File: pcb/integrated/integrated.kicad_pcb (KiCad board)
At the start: 4 copper layers, 200 x 100 mm, 264 parts, among them J10001 Conn_01x01_Female, J10002 Conn_01x01_Female, J1001 mounting-hole-grounded, J1002 mounting-hole-grounded, J1003 mounting-hole-grounded, J1004 mounting-hole-grounded, J1005 mounting-hole-grounded, J1006 mounting-hole-grounded, J3001 Conn_01x04_Male, J3002 Conn_01x06_Male, J5001 Conn_Coaxial, J8001 Conn_01x03_Female, Q10001 F423MR12W1M1B11BOMA1, Q8001 Q_NMOS_GDS, Q8002 2N7002, Q8003 Q_NMOS_GDS, U11001 UCC5350SB, U11002 R15P21503D, U12001 UCC5350SB, U12002 R15P21503D, U13001 UCC5350SB, U13002 R15P21503D, U14001 UCC5350SB, U14002 R15P21503D, U3001 XC7S25-L1FTGB196, U3002 S25FL127SABN, U3003 74AVC4TD245BQ, U5001 74LVC1G3157GW, U5002 TLV3501AIDBVR, U5003 74LVC1G3157GW, U5004 MCP6561-OT, U6001 SG3225, U6002 AD9609, U7001 AFBR-1624Z, U7002 AFBR-2624Z, U8001 VOM1271, U8002 UCC5350SB, U8003 ACS730, U9001 EC6AW, U9002 RAC10, U9003 TPS82140, U9004 TPS82140, U9005 TPS735, U9006 TPS735

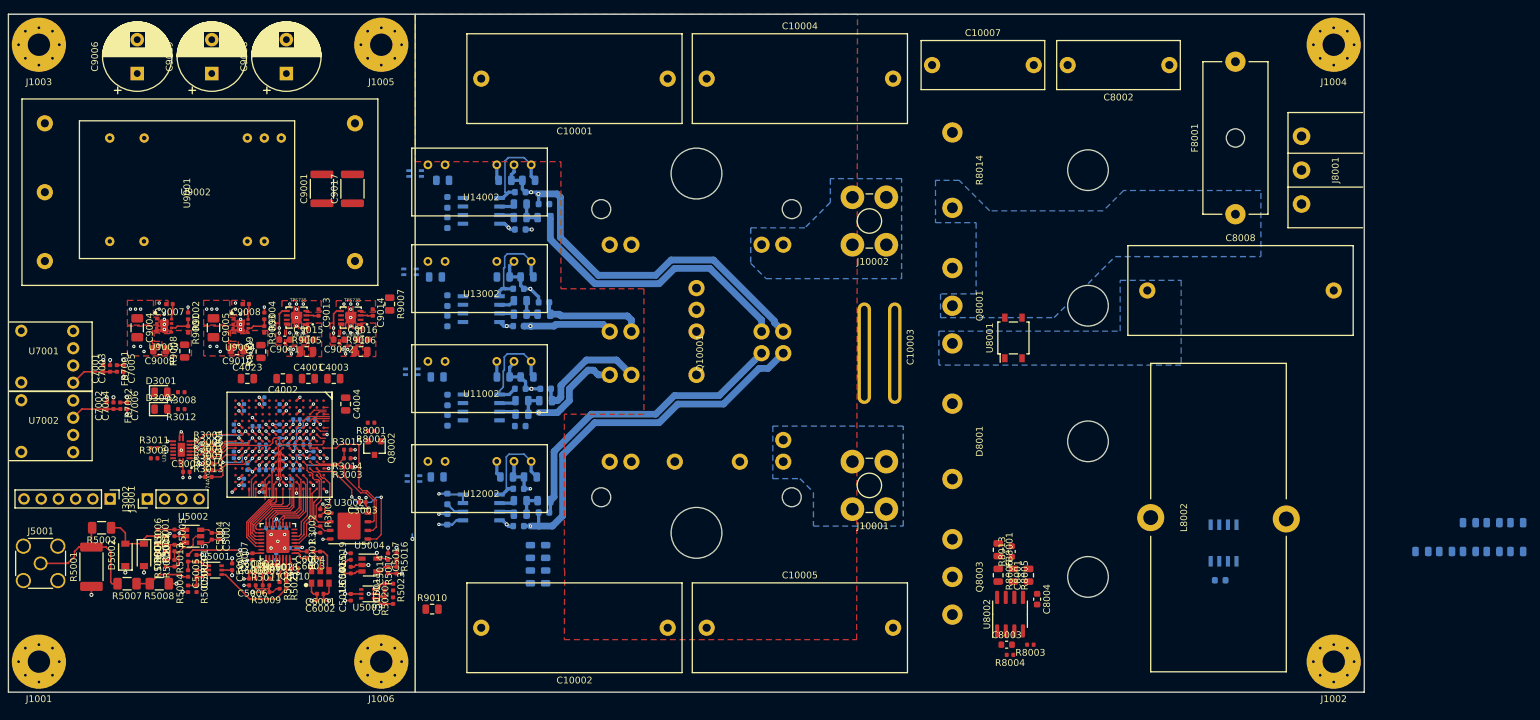
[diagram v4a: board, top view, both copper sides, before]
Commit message: redid power planes
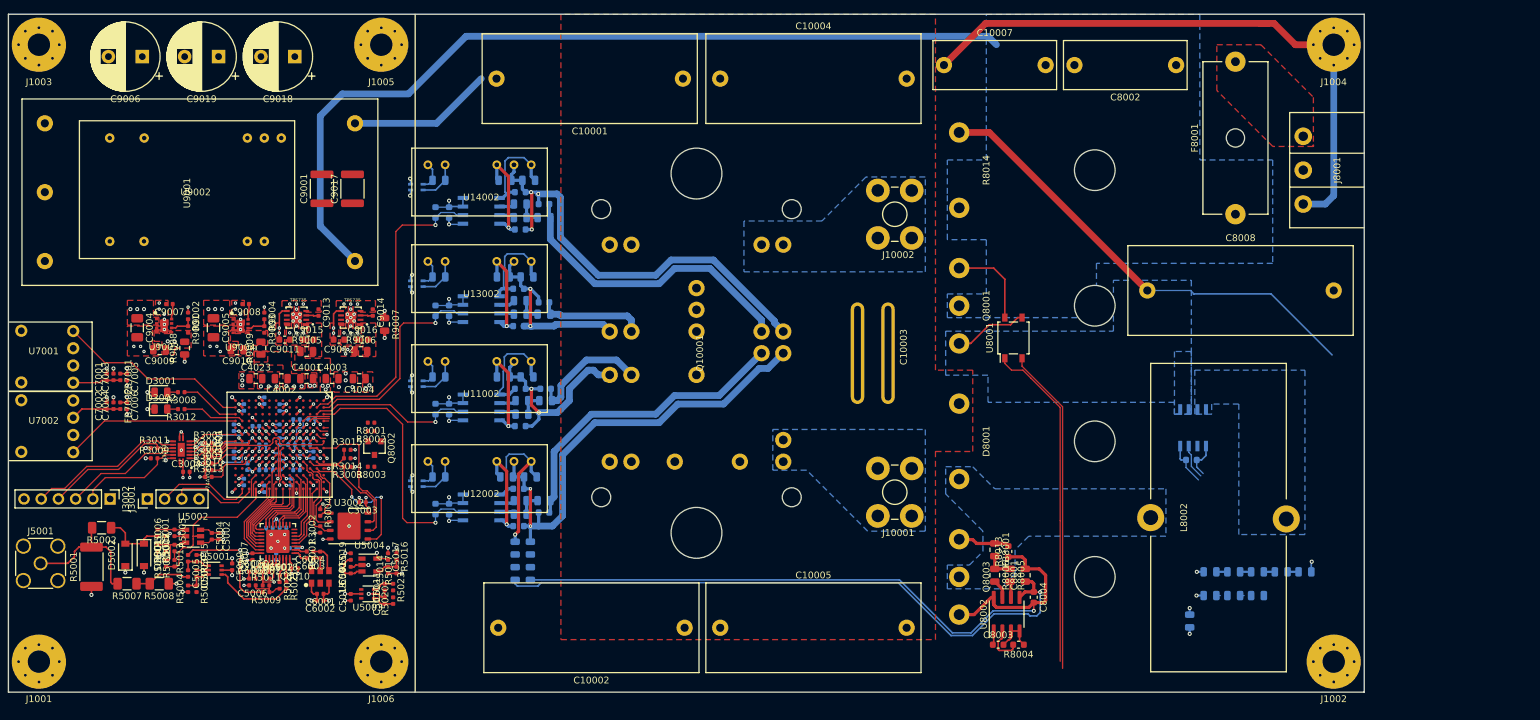
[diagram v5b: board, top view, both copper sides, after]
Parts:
- R8004: footprint Resistor_SMD:R_0402_1005Metric -> Resistor_SMD:R_0603_1608Metric
- R9010: moved to B.Cu
- moved R9010 111.8 mm to (224.2, 139.5), turned to 90 degrees
- moved R8003 100.7 mm to (103.5, 116.8)
- moved R8011 46.5 mm to (227.2, 135.8), turned to 180 degrees
- moved R10007 45.3 mm to (227.2, 132.2), turned to 180 degrees
- moved R8010 39.7 mm to (230.8, 135.8), turned to 180 degrees
- moved R10004 38.4 mm to (230.8, 132.2), turned to 180 degrees
- moved R8007 33.0 mm to (234.2, 135.8), turned to 180 degrees
- moved R10003 31.4 mm to (234.2, 132.2), turned to 180 degrees
- moved R10002 24.4 mm to (237.8, 132.2), turned to 180 degrees
- moved C8005 18.3 mm to (224.5, 115.8)
- moved U8003 17.6 mm to (224.8, 111.0)
- moved R10001 17.5 mm to (241.2, 132.2), turned to 180 degrees
- moved FB12002 4.53 mm to (124.8, 128.8)
- moved R12005 4.53 mm to (124.8, 132.5), turned to 90 degrees
- moved C4004 4.25 mm to (101.8, 103.8), turned to 180 degrees
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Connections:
- C8002 pad 1: VIN -> VLINK
- C8008 pad 1: /Power Input/S1 -> VIN
- C9001 pad 1: VIN -> VLINK
- C9017 pad 1: VIN -> VLINK
- F8001 pad 1: VIN -> VLINK
- Q8001 pad 2: VIN -> VLINK
- Q8001 pad 3: /Power Input/S1 -> VIN
- R11001 pad 2: /Inverter/Gate Drive 1/In -> GATE1
- R12001 pad 2: /Inverter/Gate Drive 2/In -> GATE2
- R13001 pad 2: /Inverter/Gate Drive 3/In -> GATE3
- R14001 pad 2: /Inverter/Gate Drive 4/In -> GATE4
- R8014 pad 1: /Power Input/S1 -> VIN
- R8014 pad 2: VIN -> VLINK
- U11001 pad 2: /Inverter/Gate Drive 1/In -> GATE1
- U12001 pad 2: /Inverter/Gate Drive 2/In -> GATE2
- U13001 pad 2: /Inverter/Gate Drive 3/In -> GATE3
- U14001 pad 2: /Inverter/Gate Drive 4/In -> GATE4
- U3001 pad A2: Net-(U3001-PadA2) -> GATE3
- U3001 pad A3: Net-(U3001-PadA3) -> GATE2
- U3001 pad B2: Net-(U3001-PadB2) -> GATE4
- U3001 pad B3: Net-(U3001-PadB3) -> GATE1
- U3001 pad L14: Net-(U3001-PadL14) -> ZCS_DETECT
- U3001 pad M14: Net-(U3001-PadM14) -> /Control/FPGA/DEBUG_RX
- U3001 pad N14: Net-(U3001-PadN14) -> /Control/FPGA/DEBUG_TX
- U3001 pad N4: Net-(U3001-PadN4) -> /Control/FPGA/LED2
- U3001 pad P2: Net-(U3001-PadP2) -> FIBER_TX
- U3001 pad P3: Net-(U3001-PadP3) -> /Control/FPGA/LED1
- U3001 pad P4: Net-(U3001-PadP4) -> FIBER_RX
- U8001 pad 3: /Power Input/S1 -> VIN
- U8003 pad 1: /Power Input/S1 -> VIN
- U8003 pad 2: /Power Input/S1 -> VIN
- U9001 pad 22: VIN -> VLINK
- U9001 pad 23: VIN -> VLINK
- U9002 pad 1: VIN -> VLINK
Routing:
- net PWRGND: track 0.00 -> 130.7 mm, vias 0 -> 4
- net VLINK: track 0.00 -> 128.7 mm
- net DRIVE_AUX+: track 0.00 -> 92.3 mm, vias 0 -> 1
- net Earth: track 0.00 -> 90.0 mm
- net VIN: track 0.00 -> 80.6 mm
- net Net-(R8003-Pad1): track 0.00 -> 49.1 mm
- net Net-(Q8002-Pad3): track 0.00 -> 48.2 mm
- net GATE4: track 0.00 -> 46.8 mm, vias 0 -> 1
- net GND: track 114.4 -> 161.2 mm, vias 130 -> 159
- net GATE2: track 0.00 -> 37.7 mm, vias 0 -> 1
- net GATE3: track 0.00 -> 31.7 mm, vias 0 -> 1
- net FIBER_TX: track 0.00 -> 28.6 mm
- net FIBER_RX: track 0.00 -> 25.8 mm
- net GATE1: track 0.00 -> 24.8 mm, vias 0 -> 1
- net Net-(J3002-Pad5): track 0.00 -> 23.2 mm
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- added copper zone on In2.Cu, net +12V
- added copper zone on In2.Cu, net +3V3
- added copper zone on In2.Cu, net /Power Rails/12_INT
- added copper zone on F.Cu, net /Power Rails/1_INT
- added copper zone on In2.Cu, net /Power Rails/5_INT
- added copper zone on B.Cu, net Net-(D8001-Pad2)
- added copper zone on F.Cu, net Net-(F8001-Pad2)
- added copper zone on B.Cu, net Net-(L8002-Pad1)
- added copper zone on In1.Cu, net PWRGND
- added copper zone on In2.Cu, net VBUS
- added copper zone on B.Cu, net VLINK
- removed copper zone on F.Cu, net +5V
- removed copper zone on B.Cu, net /Power Input/S1
- removed copper zone on In1.Cu, net GNDPWR

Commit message: PCB routing finihsed, ready for design review
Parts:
- added R5024: 33, Resistor_SMD:R_0402_1005Metric, F.Cu at (110.0, 134.5)
- added R5025: 33, Resistor_SMD:R_0402_1005Metric, F.Cu at (108.8, 134.5)
- added R5026: 33, Resistor_SMD:R_0402_1005Metric, F.Cu at (99.2, 134.0)
- added R5027: 33, Resistor_SMD:R_0402_1005Metric, F.Cu at (100.5, 134.0)
- C9001, C9017: moved to B.Cu
- R8005, R8006: value 1 -> 4.7
- moved C9001 4.47 mm to (100.2, 77.8), turned to 0 degrees
- moved R10001 3.75 mm to (241.2, 136.0)
- moved R10002 3.75 mm to (237.8, 136.0)
- moved R10003 3.75 mm to (234.2, 136.0)
- moved R10004 3.75 mm to (230.8, 136.0)
- moved R10007 3.75 mm to (227.2, 136.0)
- moved R8007 3.50 mm to (234.2, 132.2)
- moved R8010 3.50 mm to (230.8, 132.2)
- moved R8011 3.50 mm to (227.2, 132.2)
- moved C9017 2.30 mm to (100.2, 73.5), turned to 0 degrees
- moved R9010 1.52 mm to (222.8, 139.8)
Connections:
- C5015 pad 1: TEMP_B -> Net-(C5015-Pad1)
- J1001 pad 1: Earth -> Net-(J1001-Pad1)
- J1003 pad 1: Earth -> Net-(J1003-Pad1)
- J1006 pad 1: Earth -> Net-(J1006-Pad1)
- Q10001 pad T1: GND -> TEMP_A
- R5019 pad 1: TEMP_B -> Net-(C5015-Pad1)
- R5020 pad 2: VIN_SENSE -> VBUS_SENSE
- R5023 pad 2: VBUS_SENSE -> VIN_SENSE
- R8001 pad 2: Net-(R8001-Pad2) -> CHARGE_SW
- R8004 pad 2: SUPPLY_EN1 -> BOOST_SW
- U3001 pad A4: Net-(U3001-PadA4) -> BOOST_SW
- U3001 pad A5: Net-(U3001-PadA5) -> CHARGE_SW
- U5003 pad 4: XADC1_P -> Net-(R5027-Pad2)
- U5004 pad 3: TEMP_B -> Net-(C5015-Pad1)
- U8002 pad 2: SUPPLY_EN1 -> BOOST_SW
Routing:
- net +5V: track 7.60 -> 223.7 mm, vias 1 -> 2
- net Earth: track 90.0 -> 301.2 mm
- net IL_SENSE: track 5.14 -> 188.0 mm, vias 0 -> 1
- net VIN_SENSE: track 0.59 -> 147.3 mm, vias 0 -> 1
- net VBUS_SENSE: track 1.62 -> 140.8 mm, vias 0 -> 1
- net BOOST_SW: track 0.00 -> 138.7 mm, vias 0 -> 2
- net VBUS: track 1.53 -> 135.2 mm
- net Net-(Q8002-Pad3): track 48.2 -> 176.9 mm, vias 0 -> 2
- net Net-(R8003-Pad1): track 49.1 -> 172.5 mm, vias 0 -> 2
- net +3V3: track 68.5 -> 154.8 mm, vias 46 -> 49
- net TEMP_B: track 5.30 -> 58.4 mm, vias 0 -> 1
- net TEMP_A: track 0.00 -> 48.1 mm, vias 0 -> 1
- net VIN: track 80.6 -> 125.0 mm
- net GND: track 161.2 -> 191.3 mm, vias 159 -> 163
- net XADC1_N: track 5.72 -> 26.7 mm, vias 1 -> 2
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
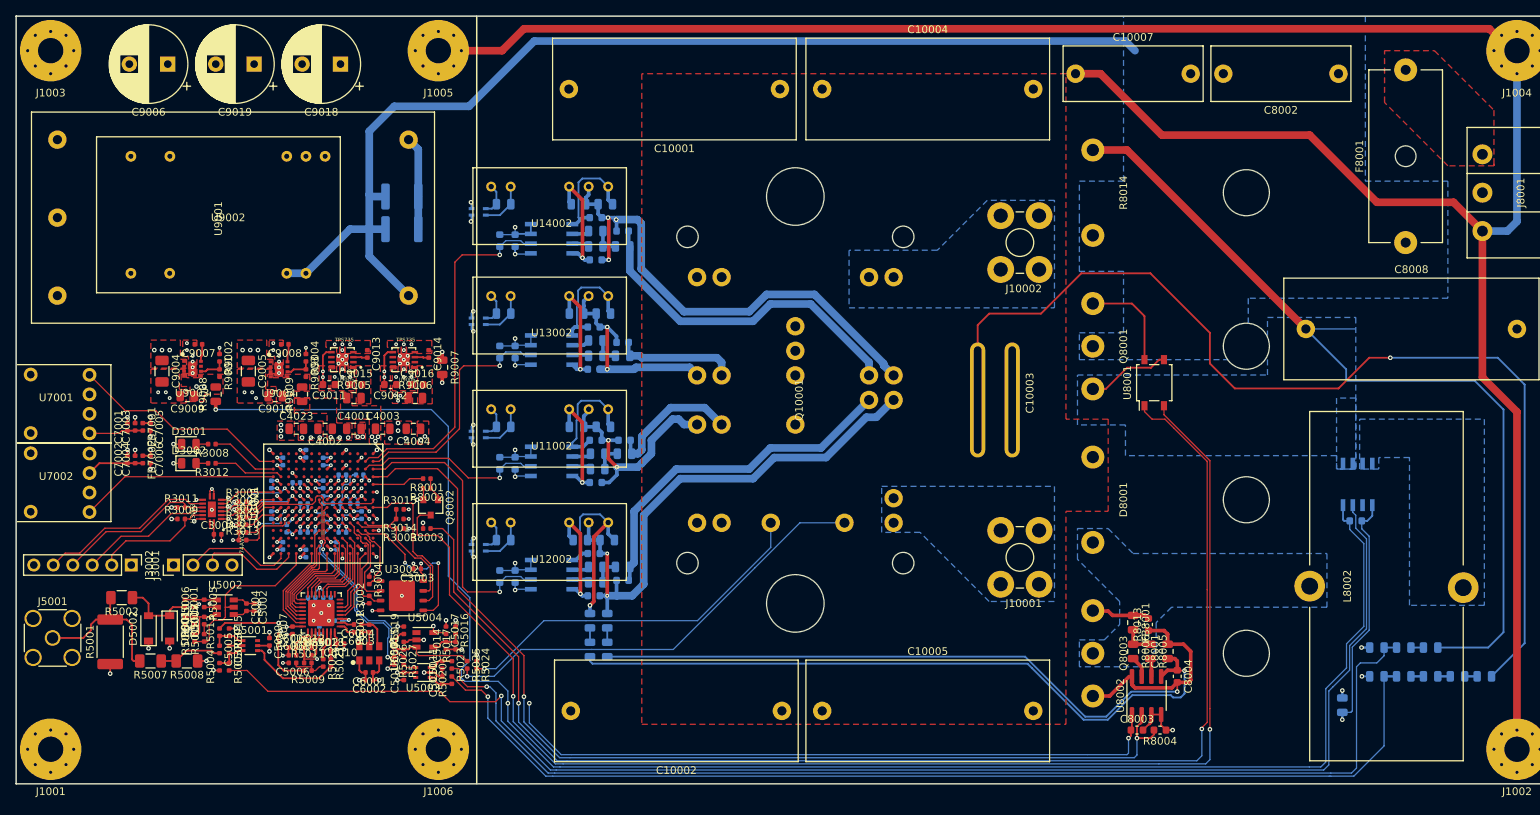
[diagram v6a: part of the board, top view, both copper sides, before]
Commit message: finished design review and sent PCB to fab
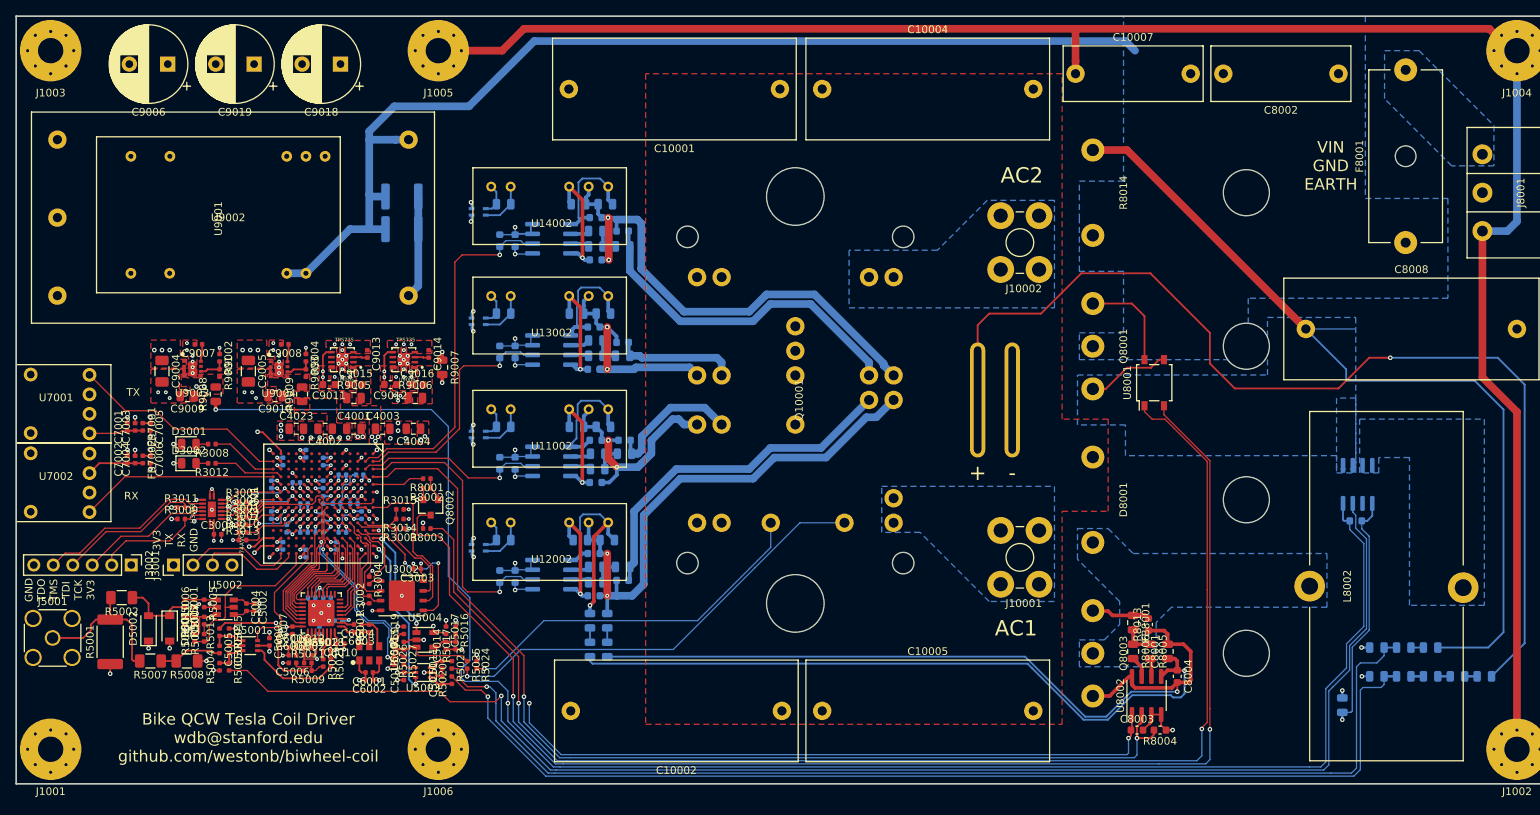
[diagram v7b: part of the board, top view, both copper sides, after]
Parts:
- C10003: moved to B.Cu
- turned C10003 to 270 degrees
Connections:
- U3001 pad A12: Net-(U3001-PadA12) -> OVER_TEMP
- U3001 pad A13: Net-(U3001-PadA13) -> ADC2_MUX_EN
- U3001 pad J13: Net-(U3001-PadJ13) -> ADC1_MUX_EN
- U9002 pad 1: VLINK -> PWRGND
- U9002 pad 2: PWRGND -> VLINK
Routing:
- net Earth: track 301.2 -> 245.6 mm
- net ADC2_MUX_EN: track 0.00 -> 21.5 mm, vias 0 -> 2
- net ADC1_MUX_EN: track 0.00 -> 17.2 mm
- net OVER_TEMP: track 0.00 -> 15.2 mm, vias 0 -> 2
- net VLINK: track 148.2 -> 142.6 mm
- net Net-(U3001-PadN1): track 0.00 -> 4.46 mm, vias 0 -> 1
- net Net-(U3001-PadP12): track 0.00 -> 3.61 mm, vias 0 -> 1
- net Net-(U3001-PadP13): track 0.00 -> 2.82 mm, vias 0 -> 1
- net VBUS_SENSE: track 140.8 -> 142.2 mm
- net PWRGND: track 121.5 -> 122.7 mm
- net /Control/FPGA/FLASH_CS: track 10.3 -> 11.1 mm
- net Net-(U3001-PadG4): track 0.00 -> 0.71 mm, vias 0 -> 1
- net /Inverter/Gate Drive 4/Source: vias 3 -> 2
- added copper zone on In2.Cu, net Net-(D8001-Pad2)
- added copper zone on B.Cu, net Net-(F8001-Pad2)
- removed copper zone on F.Cu, net Net-(F8001-Pad2)
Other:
- board text added: "+"
- board text added: "-"
- board text added: "3V3 TX RX GND"
- board text added: "AC1"
- board text added: "AC2"
- board text added: "Bike QCW Tesla Coil Driver wdb@stanford.edu github.com/westonb/biwheel-coil"
- board text added: "GND TDO TMS TDI TCK 3V3"
- board text added: "RX"
- board text added: "TX"
- board text added: "VIN GND EARTH"
